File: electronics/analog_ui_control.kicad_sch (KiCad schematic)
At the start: 2 parts, among them J3 Conn_01x08, U4 LM339_4ch

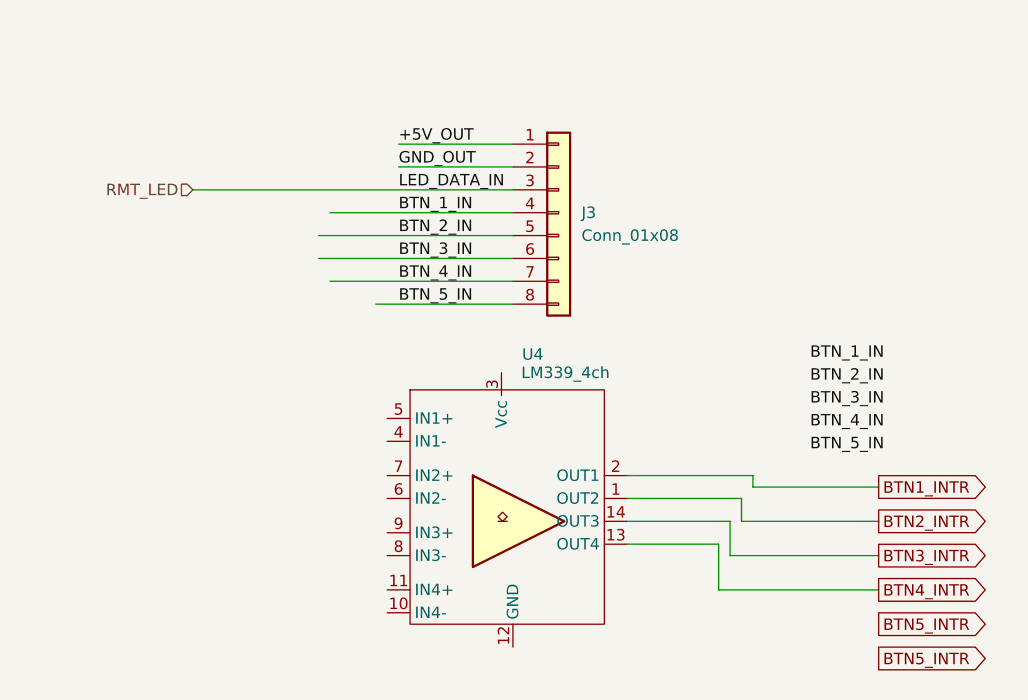
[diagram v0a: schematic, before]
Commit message: capacitors added. universal dc/dc converters
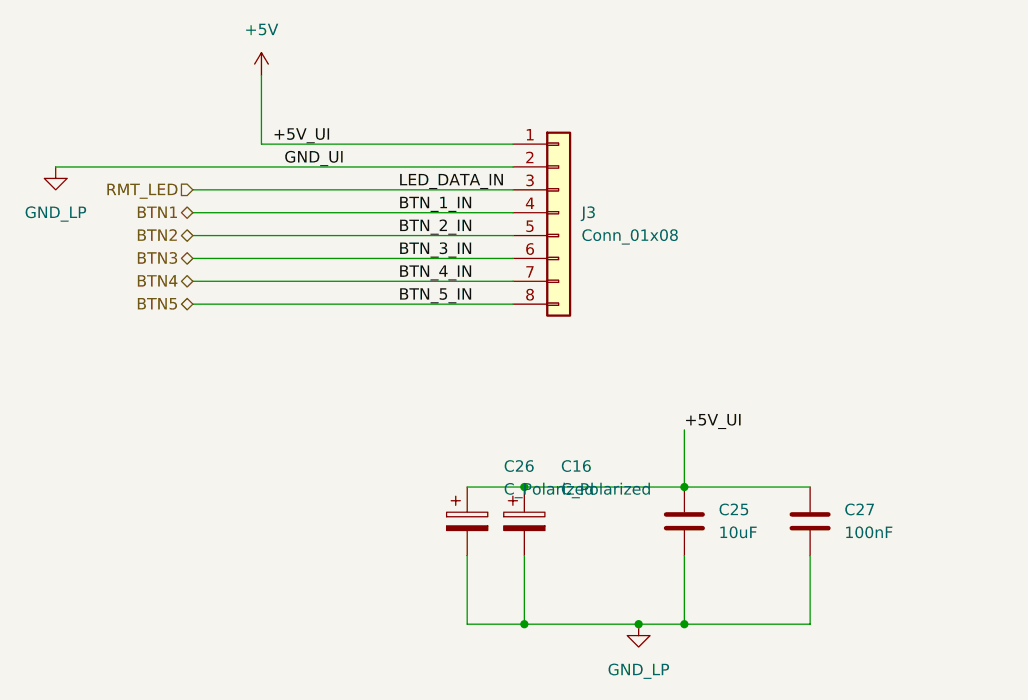
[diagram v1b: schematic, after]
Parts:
- removed U4: LM339_4ch, Package_SO:HTSSOP-14-1EP_4.4x5mm_P0.65mm_EP3.4x5mm_Mask3x3.1mm, symbol HeavyDuty:LM339_4ch
- added C16, C26: C_Polarized, Capacitor_THT:CP_Radial_D5.0mm_P2.50mm, symbol Device:C_Polarized
- added C25: 10uF, Capacitor_SMD:C_0805_2012Metric, symbol Device:C
- added C27: 100nF, Capacitor_SMD:C_0805_2012Metric, symbol Device:C
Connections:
- net +5V_OUT renamed +5V
- net +5V: now also C16.1, C25.2, C26.1, C27.2
- net BTN_1_IN renamed BTN1
- net BTN_2_IN renamed BTN2
- net BTN_3_IN renamed BTN3
- net BTN_4_IN renamed BTN4
- net BTN_5_IN renamed BTN5
- net GND_OUT renamed GND_LP
- net GND_LP: now also C16.2, C25.1, C26.2, C27.1
